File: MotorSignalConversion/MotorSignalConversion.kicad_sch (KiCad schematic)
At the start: 22 parts, among them J1 Conn_01x06_MountingPin, J2 Conn_01x02, J3 Conn_01x06_MountingPin, J4 Conn_01x04, U1 SC0915, U2 MCP4725xxx-xCH, U3 MCP4725xxx-xCH, U4 LM324

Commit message: pcb revision 1 done
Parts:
- added R7: 200K, Resistor_SMD:R_0805_2012Metric, symbol Device:R
- added U5: LSF0102DCUR, Package_SO:VSSOP-8_2.3x2mm_P0.5mm, symbol LSF0102DCUR:LSF0102DCUR
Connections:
- net 0V: no longer J2.1 (Pin_1), J2.2 (Pin_2), U4.4 (V+)
- net 3V3_OUT: now also R7.2, U5.7 (VREF_B)
- net GND: now also J2.1 (Pin_1), U5.1 (GND)
- net SpeedLeft: now also J1.4 (Pin_4)
- net SpeedReadRegulatedL: now also U5.6 (B1)
- net SpeedReadRegulatedR: now also U5.5 (B2)
- net SpeedReadUL: now also U5.3 (A1)
- net SpeedReadUR: now also U5.4 (A2)
- net SpeedRight: now also J3.4 (Pin_4)
- net 5V_OUT: now reaches U1.40 (VBUS)
- net 5V_OUT: now also U5.2 (VREF_A)
- removed net RefSpeed: J1.4 (Pin_4), J3.4 (Pin_4)
- new net: R7.1, U5.8 (EN)
- new net 12V: J2.2 (Pin_2), U4.4 (V+)

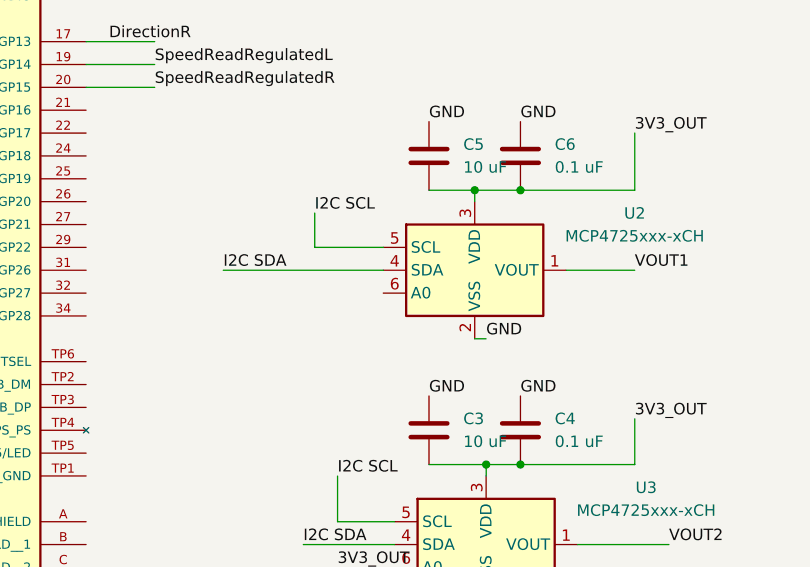
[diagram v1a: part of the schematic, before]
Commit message: added the manufacturer numbers, ready to export a 3d models
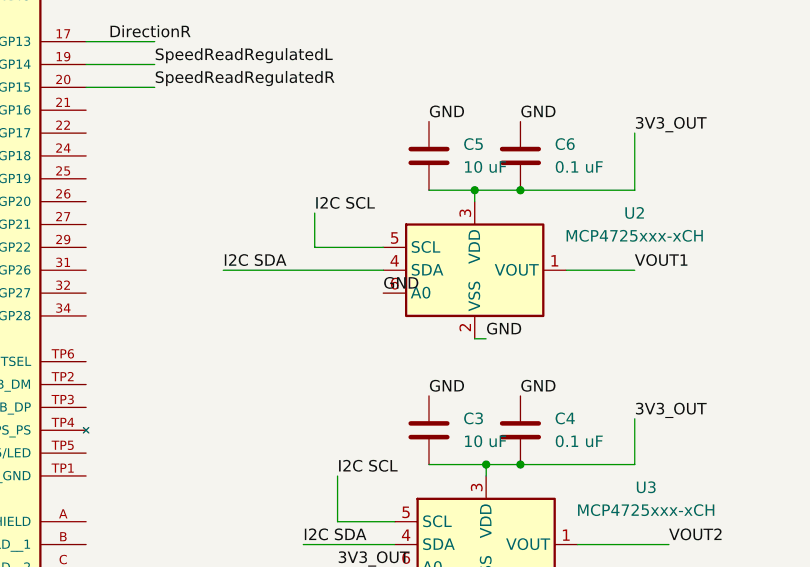
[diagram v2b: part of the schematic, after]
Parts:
- C3, C5: Manufacturer Part Number (none) -> GRM21BR61C106KE15K
- C4, C6: Manufacturer Part Number (none) -> CC0805KRX7R9BB104
- J1, J3: Manufacturer Part Number (none) -> S6B-PH-SM4-TB
- J2: Manufacturer Part Number (none) -> B4B-PH-SM4-TB
- J4: Manufacturer Part Number (none) -> B2B-PH-SM4-TB
- R1, R2: Manufacturer Part Number (none) -> CRCW08054K70FKEAC
- R3, R5: Manufacturer Part Number (none) -> RC0805FR-07909RL
- R4, R6: Manufacturer Part Number (none) -> RC0805FR-072K1L
- R7: Manufacturer Part Number (none) -> ERA-6AEB204V
- U1: Manufacturer Part Number (none) -> SC0915
- U2, U3: Manufacturer Part Number (none) -> SOT-23-6 MCP4725A1T-E/CH
- U4: Manufacturer Part Number (none) -> LM324PWR
- U5: Manufacturer Part Number (none) -> LSF0102DCUR
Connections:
- net GND: now also U2.6 (A0)

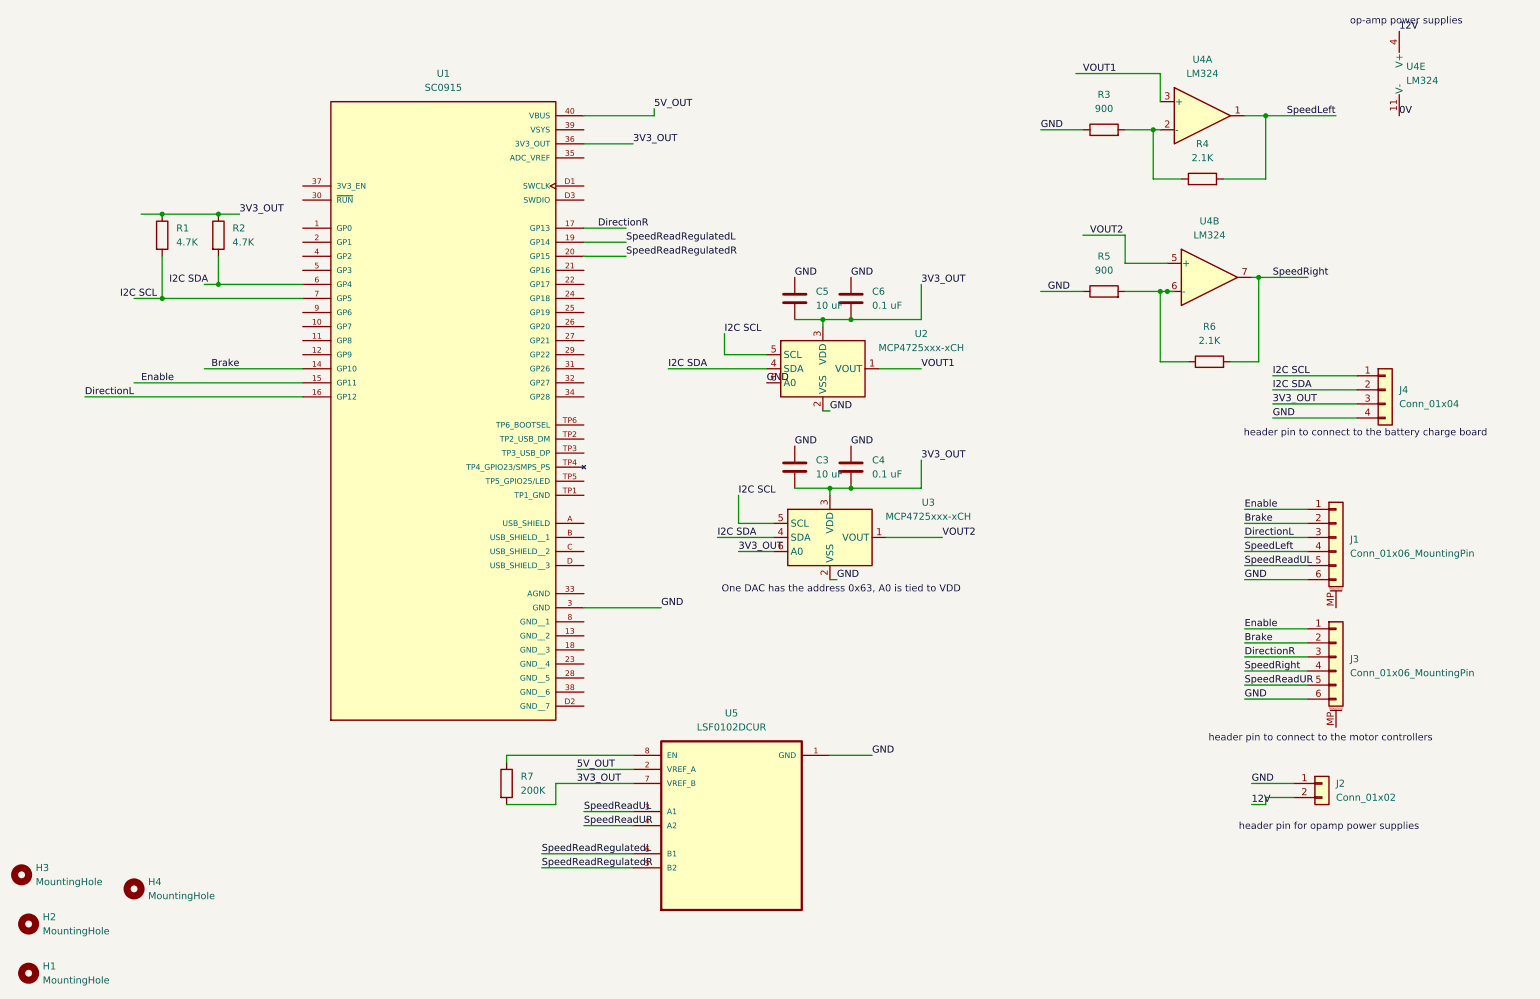
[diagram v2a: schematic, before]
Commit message: added the schematic for the battery circuit
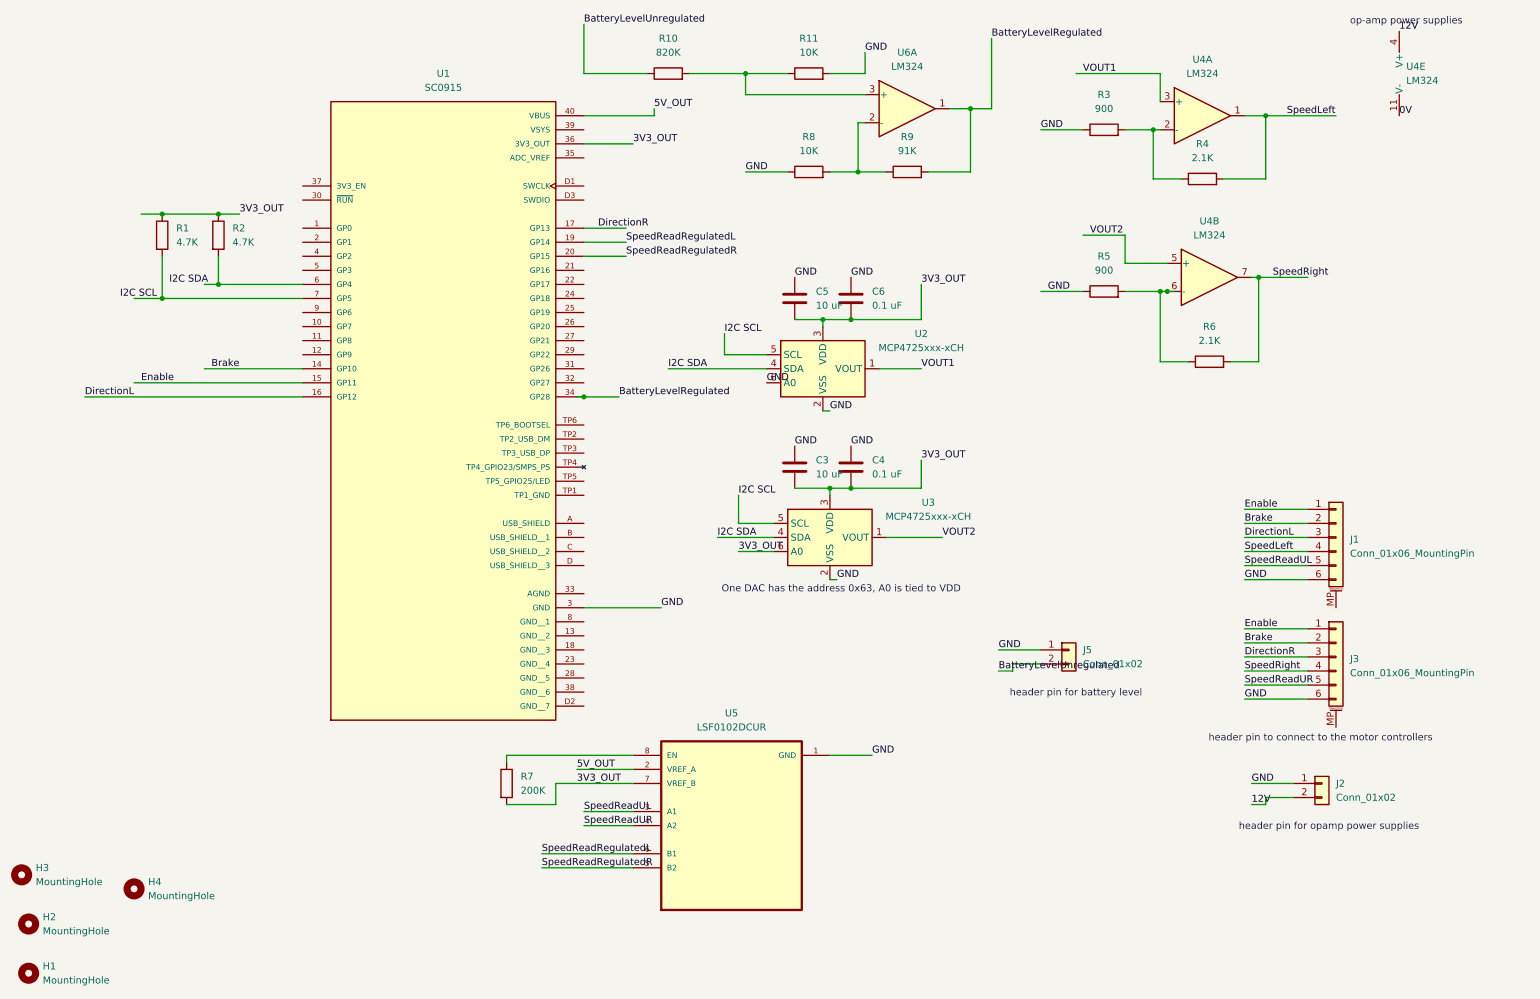
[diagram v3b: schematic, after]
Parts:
- removed J4: Conn_01x04, Connector_JST:JST_PH_B4B-PH-SM4-TB_1x04-1MP_P2.00mm_Vertical, symbol Connector_Generic:Conn_01x04
- added J5: Conn_01x02, Connector_JST:JST_PH_B2B-PH-SM4-TB_1x02-1MP_P2.00mm_Vertical, symbol Connector_Generic:Conn_01x02
- added R10: 820K, Resistor_SMD:R_0805_2012Metric, symbol Device:R
- added R11, R8: 10K, Resistor_SMD:R_0805_2012Metric, symbol Device:R
- added R9: 91K, Resistor_SMD:R_0805_2012Metric, symbol Device:R
- added U6: LM324, Package_SO:TSSOP-14_4.4x5mm_P0.65mm, symbol Amplifier_Operational:LM324
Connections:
- net GND: now also J5.1 (Pin_1), R11.2, R8.1
- net BatteryLevelRegulated: now reaches U1.34 (GP28)
- net BatteryLevelRegulated: now also R9.2, U6.1
- new net: R8.2, R9.1, U6.2 (-)
- new net: R10.2, R11.1, U6.3 (+)
- new net BatteryLevelUnregulated: J5.2 (Pin_2), R10.1
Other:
- note added: "header pin for battery level"
- note removed: "header pin to connect to the battery charge board"

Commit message: revised based on feedback
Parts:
- renumbered U6 to U4
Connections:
- net 0V is gone; now on net GND: U4.11 (V-)
- net BatteryLevelRegulated: now also U4.8; no longer U4.1
- net I2C SCL: now also R1.2, U1.7 (GP5)
- net I2C SDA: now also R2.2, U1.6 (GP4)
- net at R8.2, R9.1: now also U4.9 (-); no longer U4.2 (-)
- net at R10.2, R11.1: now also U4.10 (+); no longer U4.3 (+)
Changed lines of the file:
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@@
 		)
 	)
-	(label "0V"
+	(label "GND"
 		(at 266.7 35.56 0)
 		(fields_autoplaced yes)
@@
 	)
 	(label "I2C SDA"
-		(at 44.45 66.04 0)
+		(at 50.8 66.04 0)
 		(fields_autoplaced yes)
 		(effects
@@
 	)
 	(label "I2C SCL"
-		(at 35.56 68.58 0)
+		(at 38.1 68.58 0)
 		(fields_autoplaced yes)
 		(effects
@@
 		(lib_id "Amplifier_Operational:LM324")
 		(at 177.8 34.29 0)
-		(unit 1)
+		(unit 3)
 		(exclude_from_sim no)
 		(in_bom yes)
@@
 		(dnp no)
 		(fields_autoplaced yes)
-		(property "Reference" "U6"
+		(property "Reference" "U4"
 			(at 177.8 24.13 0)
 			(effects
@@
 			(project "MotorSignalConversion"
 				(path "/0366205a-f6c1-4cb9-aac8-32bb3f1e3d88"
-					(reference "U6")
-					(unit 1)
-				)
-			)
+					(reference "U4")
+					(unit 3)
+				)
+			)
